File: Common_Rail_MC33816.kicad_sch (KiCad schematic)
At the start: 181 parts, among them J10 INJ_Term, J11 INJ_Term, J12 INJ_Term, J14 CONN_01X03, J15 CONN_01X01, J20 Conn_01x02, J5 CONN_01X03, J6 CONN_01X03, J7 CONN_01X03, J8 INJ_Term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

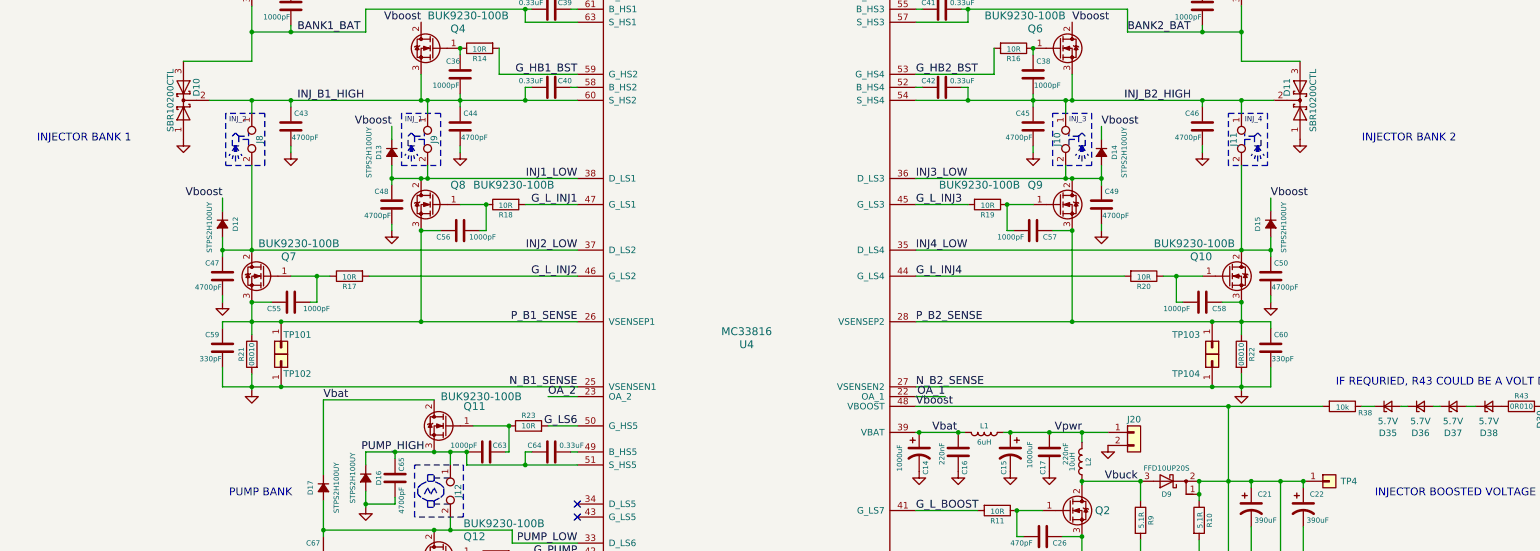
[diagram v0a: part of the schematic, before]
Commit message: Added injector net names to the sheet labels.
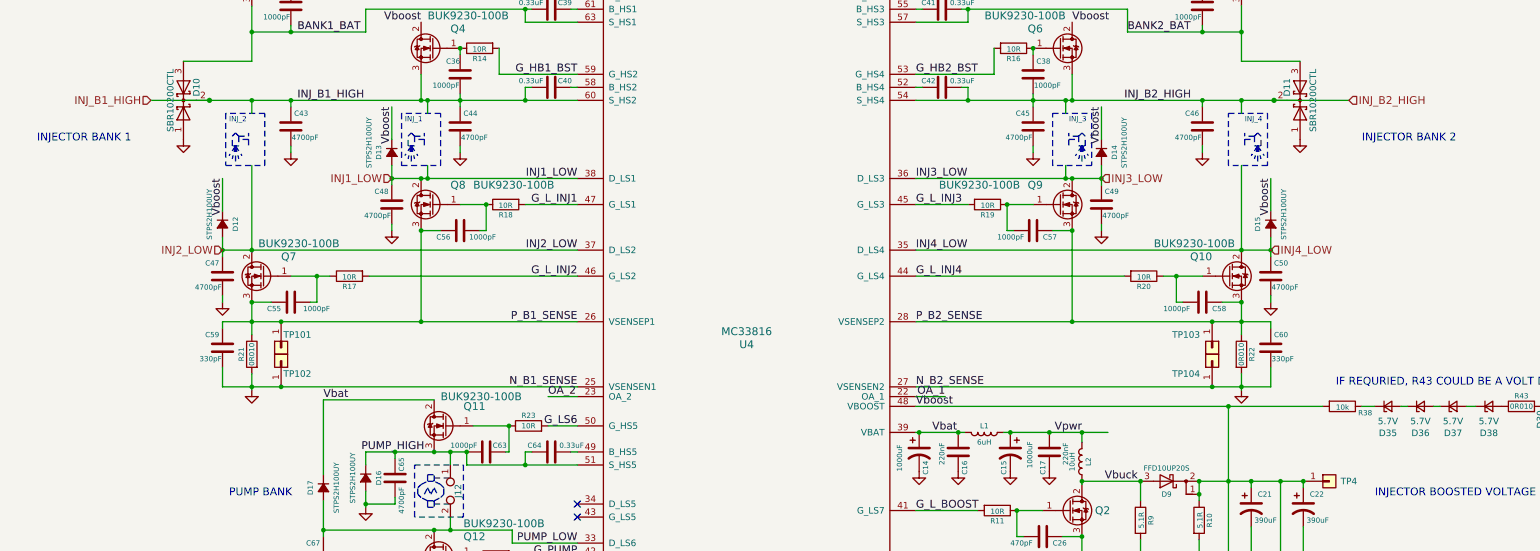
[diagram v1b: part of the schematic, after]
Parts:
- removed J10, J11, J9: INJ_Term, TerminalBlock:TerminalBlock_bornier-2_P5.08mm, symbol Connector:TestPoint_2Pole
- removed J20: Conn_01x02, TerminalBlock:TerminalBlock_bornier-2_P5.08mm, symbol Connector_Generic:Conn_01x02
- removed J8: INJ_Term, Terminal_Blocks:TerminalBlock_bornier-2_P5.08mm, symbol Connector:TestPoint_2Pole
